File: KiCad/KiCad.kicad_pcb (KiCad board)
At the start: 2 copper layers, 100 x 46.3 mm, 48 parts, among them J1 DC-IN, J2 TYPE-C, J3 Conn_01x03_Pin, J4 Conn_01x03_Pin, J5 Conn_01x03_Pin, J6 Conn_01x03_Pin, Q1 IRF3708, SW1 reset, SW2 start, U1 ESP32-WROOM-32E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

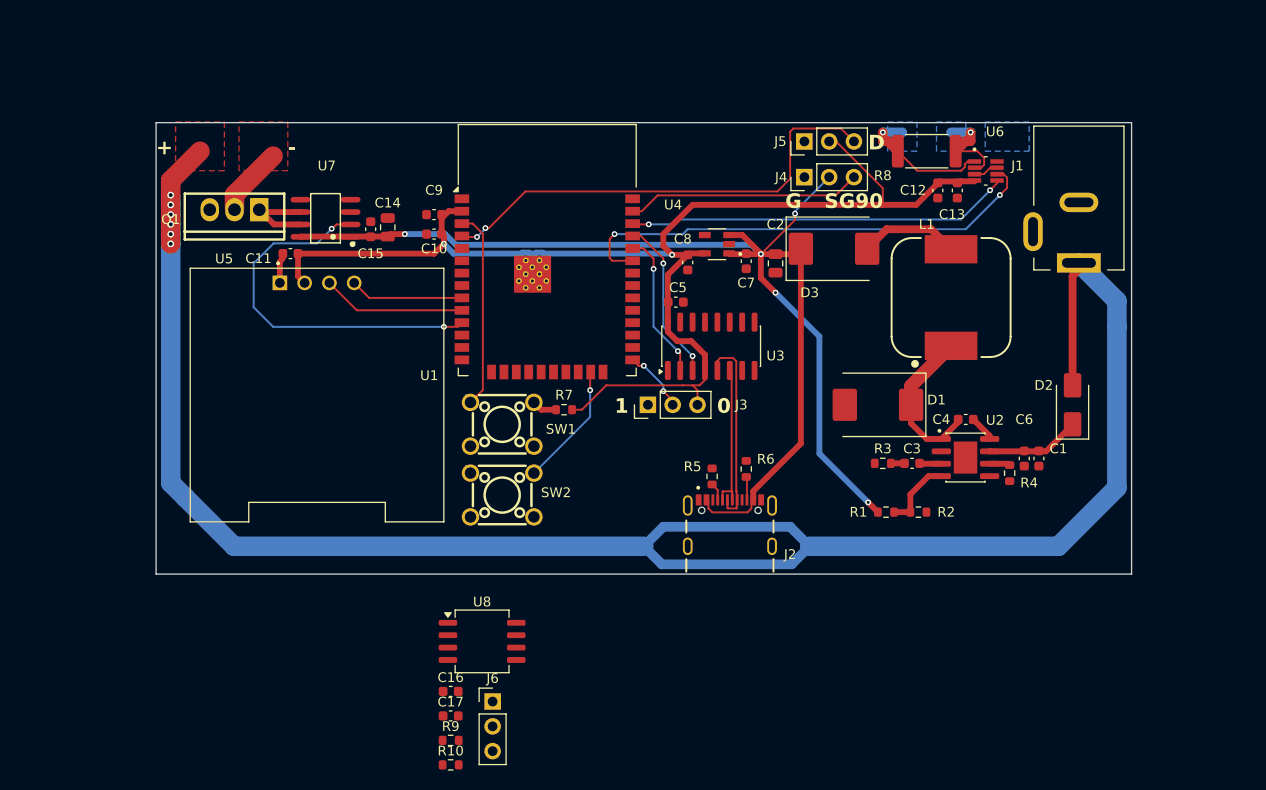
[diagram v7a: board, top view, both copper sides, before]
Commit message: 完成PCB及原理圖所有的連接
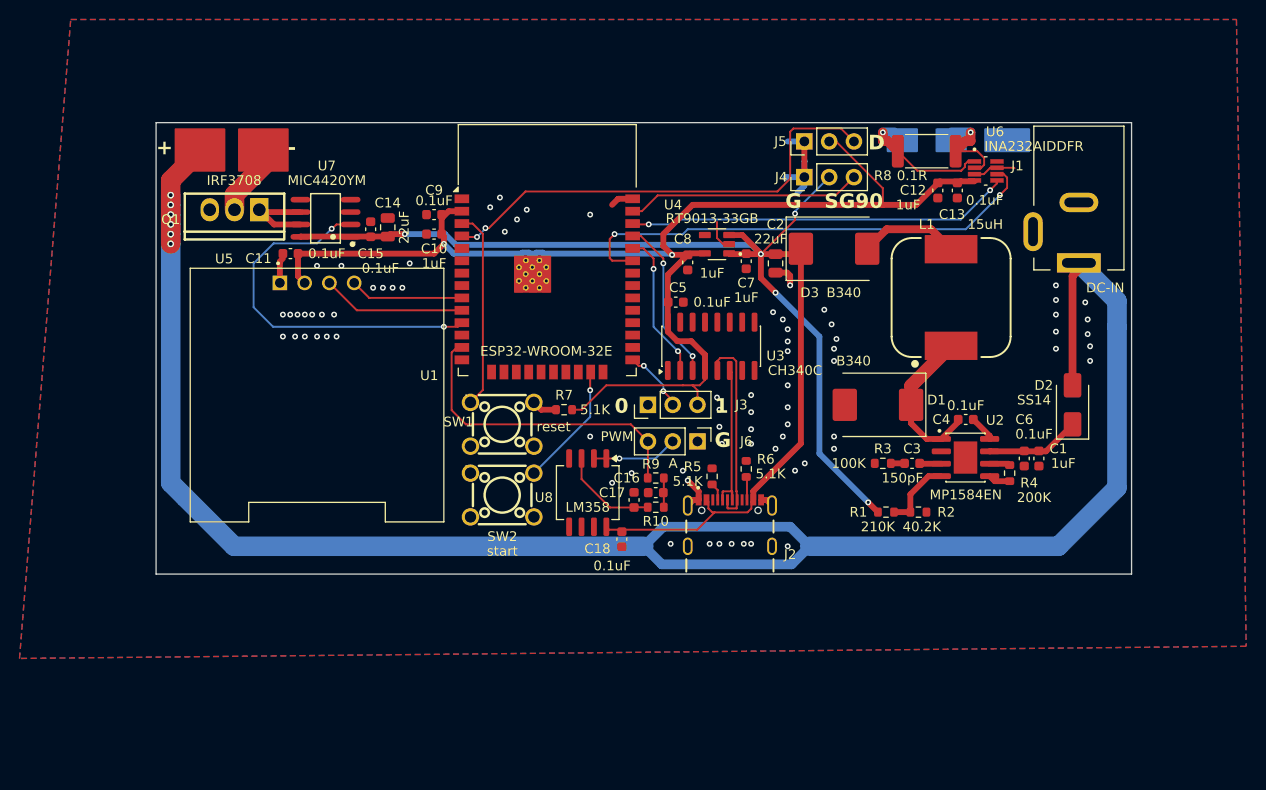
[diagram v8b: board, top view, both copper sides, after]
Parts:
- added C18: 0.1uF, Capacitor_SMD:C_0603_1608Metric, F.Cu at (205.8, 102.8)
- R10, R9: value 5.1K -> 10K
- moved R9 34.1 mm to (209.2, 96.5)
- moved J6 33.9 mm to (213.5, 92.8), turned to -90 degrees
- moved R10 33.8 mm to (209.2, 99.5), turned to 180 degrees
- moved C16 29.3 mm to (209.2, 98.0), turned to 180 degrees
- moved C17 29.0 mm to (207.0, 98.8), turned to 90 degrees
- moved U8 18.7 mm to (202.2, 98.0), turned to -90 degrees
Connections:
- J6 pad 1: unconnected-(J6-Pin_1-Pad1) -> GND
- J6 pad 3: unconnected-(J6-Pin_3-Pad3) -> /BUCK_PWM
- U1 pad 13: unconnected-(U1-IO14-Pad13) -> /BUCK_PWM
- U8 pad 2: Net-(U8A-+) -> Net-(J6-Pin_2)
- U8 pad 8: +3V3 -> +5V
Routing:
- net /BUCK_PWM: track 0.00 -> 32.4 mm
- net GND: track 5.76 -> 34.1 mm, vias 0 -> 76
- net +5V: track 136.5 -> 148.5 mm
- net Net-(U8A-+): track 0.00 -> 10.1 mm
- net Net-(J6-Pin_2): track 0.00 -> 8.80 mm, vias 0 -> 1
- net Net-(C16-Pad1): track 0.00 -> 3.00 mm
- net /IN+: track 14.1 -> 13.3 mm
- added copper zone on F.Cu, net GND
- removed copper zone on B.Cu, net /IN+
- removed copper zone on B.Cu, net /IN-
- removed copper zone on F.Cu, net /MOTOR
- removed copper zone on F.Cu, net VCC
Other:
- board text added: "A"
- board text added: "PWM"
